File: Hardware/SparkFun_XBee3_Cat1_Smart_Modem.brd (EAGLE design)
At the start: 45.7 x 63.5 mm, 138 parts, among them J1 USB Female Type C Connector, J3 USB Female Type C Connector, J4 QWIIC_RIGHT_ANGLE, Q2 3.1A/30V/105mΩ, U1 FSUSB30MUX_MSOP10, U2 AP63203, U3 ESD Diode, U5 ESD Diode, U7 FT231XS

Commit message: Adds a few more vias
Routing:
- net GND: vias 80 -> 82
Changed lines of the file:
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@@
 <via x="17.1196" y="15.0368" extent="1-16" drill="0.3048"/>
 <via x="27.9146" y="15.0622" extent="1-16" drill="0.3048"/>
+<via x="27.6606" y="13.6906" extent="1-16" drill="0.3048"/>
+<via x="30.0482" y="12.6492" extent="1-16" drill="0.3048"/>
 </signal>
 <signal name="3.3V">
@@
 <wire x1="27.94" y1="33.401" x2="28.0924" y2="33.401" width="0.762" layer="16"/>
 <wire x1="28.0924" y1="33.401" x2="28.8544" y2="32.639" width="0.762" layer="16"/>
-<wire x1="30.099" y1="26.543" x2="29.7948" y2="29.21" width="0" layer="19" extent="1-1"/>
-<wire x1="33.108" y1="21.971" x2="33.147" y2="23.114" width="0" layer="19" extent="1-1"/>
-<wire x1="13.12" y1="19.304" x2="13.081" y2="20.447" width="0" layer="19" extent="1-1"/>
-<wire x1="28.917" y1="25.781" x2="30.099" y2="25.654" width="0" layer="19" extent="1-1"/>
-<wire x1="31.662" y1="13.589" x2="30.48" y2="13.589" width="0" layer="19" extent="1-1"/>
-<wire x1="28.917" y1="24.2824" x2="30.099" y2="24.638" width="0" layer="19" extent="1-1"/>
-<wire x1="33.3375" y1="20.4597" x2="33.108" y2="21.971" width="0" layer="19" extent="1-1"/>
-<wire x1="31.4325" y1="15.1003" x2="31.662" y2="13.589" width="0" layer="19" extent="1-1"/>
-<wire x1="30.7975" y1="15.1003" x2="31.4325" y2="15.1003" width="0" layer="19" extent="1-1"/>
-<wire x1="30.1625" y1="15.1003" x2="30.7975" y2="15.1003" width="0" layer="19" extent="1-1"/>
-<wire x1="13.12" y1="17.78" x2="13.12" y2="19.304" width="0" layer="19" extent="1-1"/>
 </signal>
 <signal name="V_USB">
@@
 <vertex x="23.622" y="29.591"/>
 </polygon>
-<wire x1="26.6448" y1="29.21" x2="26.25" y2="32.512" width="0" layer="19" extent="1-1"/>
-<wire x1="24.2351" y1="29.21" x2="26.6448" y2="29.21" width="0" layer="19" extent="1-1"/>
 </signal>
 <signal name="EN">

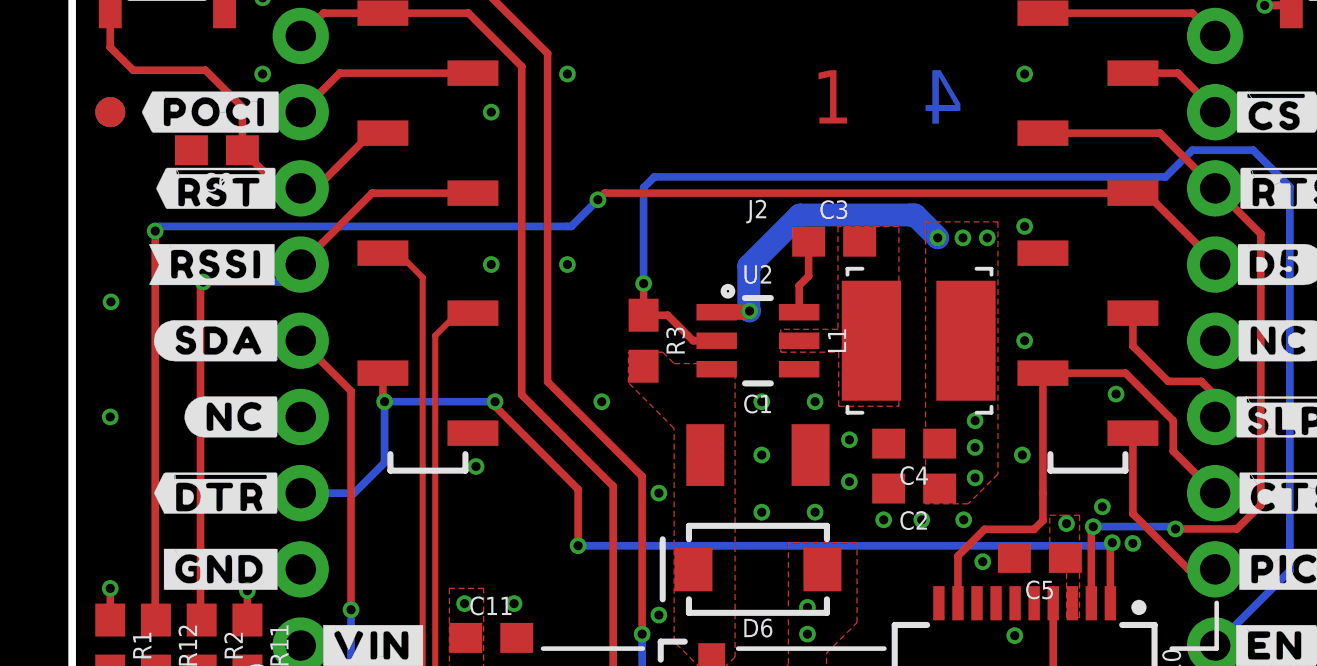
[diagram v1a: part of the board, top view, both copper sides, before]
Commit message: Updates inductor to one with a higher saturation rating
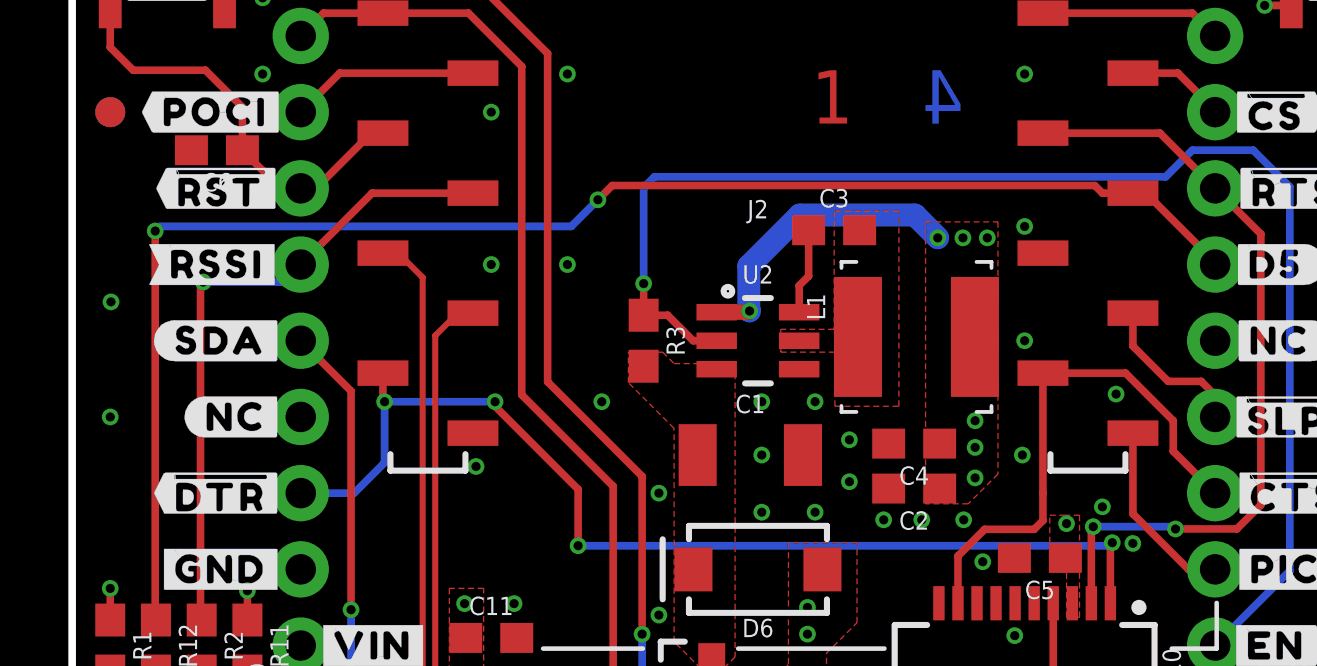
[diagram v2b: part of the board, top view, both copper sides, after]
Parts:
- L1: value 3.9uH -> 3.9UH
- moved C3 0.38 mm to (25.4, 32.9)
- moved C1 0.25 mm to (22.6, 25.4)
- moved L1 0.14 mm to (28.2, 29.3), turned to 270 degrees
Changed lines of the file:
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@@
 <setting verticaltext="up"/>
 </settings>
-<grid distance="0.05" unitdist="inch" unit="inch" style="dots" multiple="1" display="yes" altdistance="0.001" altunitdist="inch" altunit="inch"/>
+<grid distance="0.05" unitdist="inch" unit="inch" style="dots" multiple="1" display="yes" altdistance="0.005" altunitdist="inch" altunit="inch"/>
 <layers>
 <layer number="1" name="Top" color="4" fill="1" visible="yes" active="yes"/>
@@
 <layer number="39" name="tKeepout" color="4" fill="11" visible="yes" active="yes"/>
 <layer number="40" name="bKeepout" color="1" fill="11" visible="no" active="yes"/>
-<layer number="41" name="tRestrict" color="4" fill="10" visible="no" active="yes"/>
+<layer number="41" name="tRestrict" color="4" fill="10" visible="yes" active="yes"/>
 <layer number="42" name="bRestrict" color="1" fill="10" visible="no" active="yes"/>
 <layer number="43" name="vRestrict" color="2" fill="10" visible="no" active="yes"/>
@@
 <wire x1="25.146" y1="1.524" x2="26.67" y2="0" width="0.2032" layer="20" curve="-90"/>
 <text x="24.257" y="1.905" size="1.27" layer="16" font="vector" ratio="15" rot="MR0">v10</text>
-<rectangle x1="27.8384" y1="32.8422" x2="28.0924" y2="33.0962" layer="41"/>
+<rectangle x1="27.8384" y1="33.0962" x2="28.0924" y2="33.3502" layer="41"/>
 <text x="20.447" y="0.381" size="0.762" layer="46" font="vector" ratio="15">Route Out</text>
 <dimension x1="38.1" y1="44.45" x2="0" y2="44.45" x3="19.05" y3="74.93" textsize="1.778" textratio="15" layer="47" unit="inch"/>
@@
 <attribute name="VALUE" x="22.86" y="26.67" size="0.6096" layer="27" font="vector" ratio="20" align="bottom-center"/>
 </element>
-<element name="L1" library="SparkFun-Coils" package="INDUCTOR_3.9UH" value="3.9uH" x="28.2448" y="29.21" smashed="yes" rot="R90">
-<attribute name="NAME" x="25.8028" y="29.21" size="0.6096" layer="25" font="vector" ratio="20" rot="R90" align="bottom-center"/>
-<attribute name="PROD_ID" value="NDUC-18014" x="25.7048" y="22.86" size="1.778" layer="27" rot="R90" display="off"/>
-<attribute name="VALUE" value="3.9uH" x="30.6578" y="29.21" size="0.6096" layer="27" font="vector" ratio="20" rot="R90" align="top-center"/>
-</element>
-<element name="C3" library="SparkFun-Capacitors" package="0603" value="0.1uF" x="25.4" y="32.512" smashed="yes">
-<attribute name="NAME" x="25.4" y="33.274" size="0.6096" layer="25" font="vector" ratio="20" align="bottom-center"/>
-<attribute name="PROD_ID" value="CAP-08604" x="13.97" y="35.052" size="1.778" layer="27" display="off"/>
-<attribute name="VALUE" x="25.4" y="31.75" size="0.6096" layer="27" font="vector" ratio="20" align="top-center"/>
+<element name="C3" library="SparkFun-Capacitors" package="0603" value="0.1uF" x="25.4" y="32.893" smashed="yes">
+<attribute name="NAME" x="25.4" y="33.655" size="0.6096" layer="25" font="vector" ratio="20" align="bottom-center"/>
+<attribute name="PROD_ID" value="CAP-08604" x="13.97" y="35.433" size="1.778" layer="27" display="off"/>
+<attribute name="VALUE" x="25.4" y="32.131" size="0.6096" layer="27" font="vector" ratio="20" align="top-center"/>
 </element>
 <element name="C2" library="SparkFun-Capacitors" package="0603" value="22uF" x="28.067" y="24.2824" smashed="yes" rot="R180">
@@
 <attribute name="VALUE" x="28.067" y="26.543" size="0.6096" layer="27" font="vector" ratio="20" rot="R180" align="top-center"/>
 </element>
-<element name="C1" library="SparkFun-Capacitors" package="1210" value="10uF" x="22.86" y="25.4" smashed="yes">
-<attribute name="NAME" x="22.86" y="26.797" size="0.6096" layer="25" font="vector" ratio="20" align="bottom-center"/>
-<attribute name="PROD_ID" value="CAP-09824" x="12.7" y="8.89" size="1.778" layer="27" display="off"/>
-<attribute name="VALUE" x="22.86" y="24.003" size="0.6096" layer="27" font="vector" ratio="20" align="top-center"/>
+<element name="C1" library="SparkFun-Capacitors" package="1210" value="10uF" x="22.606" y="25.4" smashed="yes">
+<attribute name="NAME" x="22.606" y="26.797" size="0.6096" layer="25" font="vector" ratio="20" align="bottom-center"/>
+<attribute name="PROD_ID" value="CAP-09824" x="12.446" y="8.89" size="1.778" layer="27" display="off"/>
+<attribute name="VALUE" x="22.606" y="24.003" size="0.6096" layer="27" font="vector" ratio="20" align="top-center"/>
 </element>
 <element name="R3" library="SparkFun-Resistors" package="0603" value="10k" x="19.05" y="29.21" smashed="yes" rot="R270">
@@
 <attribute name="PROD_ID" value="CAP-00810" x="32.258" y="21.971" size="1.778" layer="27" font="vector" ratio="15" rot="R180" display="off"/>
 <attribute name="VALUE" x="32.258" y="22.733" size="0.6096" layer="27" font="vector" ratio="20" rot="R180" align="top-center"/>
+</element>
+<element name="L1" library="SparkFun-Coils" package="INDUCTOR_3.9UH" value="3.9UH" x="28.194" y="29.337" smashed="yes" rot="R270">
+<attribute name="NAME" x="24.494" y="30.787" size="0.6096" layer="25" font="vector" ratio="20" rot="R270"/>
+<attribute name="VALUE" x="31.194" y="31.037" size="0.6096" layer="27" font="vector" ratio="20" rot="R270"/>
 </element>
 </elements>
@@
 <contactref element="J4" pad="2"/>
 <contactref element="R11" pad="1"/>
-<contactref element="L1" pad="P$2"/>
 <contactref element="C4" pad="1"/>
 <contactref element="C2" pad="1"/>
@@
 <wire x1="22.5806" y1="30.2006" x2="22.5552" y2="30.226" width="0.762" layer="16"/>
 <wire x1="22.5552" y1="31.6992" x2="22.5552" y2="30.226" width="0.762" layer="16"/>
-<wire x1="24.257" y1="33.401" x2="27.94" y2="33.401" width="0.762" layer="16"/>
+<wire x1="24.257" y1="33.401" x2="28.0924" y2="33.401" width="0.762" layer="16"/>
 <contactref element="J6" pad="1"/>
 <wire x1="22.5552" y1="31.6992" x2="24.257" y2="33.401" width="0.762" layer="16"/>
@@
 <contactref element="U7" pad="14"/>
 <contactref element="U7" pad="13"/>
-<wire x1="27.94" y1="33.401" x2="28.0924" y2="33.401" width="0.762" layer="16"/>
 <wire x1="28.0924" y1="33.401" x2="28.8544" y2="32.639" width="0.762" layer="16"/>
+<contactref element="L1" pad="P$2"/>
 </signal>
 <signal name="V_USB">
@@
 <contactref element="J2" pad="15"/>
 <via x="17.526" y="33.909" extent="1-16" drill="0.3048"/>
-<wire x1="35.36" y1="34.13" x2="17.747" y2="34.13" width="0.254" layer="1"/>
-<wire x1="17.526" y1="33.909" x2="17.747" y2="34.13" width="0.254" layer="1"/>
+<wire x1="35.36" y1="34.13" x2="34.344" y2="34.13" width="0.254" layer="1"/>
+<wire x1="34.344" y1="34.13" x2="34.09" y2="34.384" width="0.254" layer="1"/>
+<wire x1="34.09" y1="34.384" x2="18.001" y2="34.384" width="0.254" layer="1"/>
+<wire x1="17.526" y1="33.909" x2="18.001" y2="34.384" width="0.254" layer="1"/>
 <contactref element="J5" pad="6"/>
 <wire x1="38.1" y1="31.8218" x2="35.7918" y2="34.13" width="0.254" layer="1"/>
@@
 <wire x1="2.794" y1="19.9" x2="2.7686" y2="19.9254" width="0.254" layer="1"/>
 <via x="2.7686" y="32.8676" extent="1-16" drill="0.3048"/>
-<wire x1="16.51" y1="33.02" x2="2.921" y2="33.02" width="0.254" layer="16"/>
+<wire x1="16.637" y1="33.02" x2="2.921" y2="33.02" width="0.254" layer="16"/>
 <wire x1="2.7686" y1="32.8676" x2="2.921" y2="33.02" width="0.254" layer="16"/>
 <wire x1="35.36" y1="34.13" x2="35.7918" y2="34.13" width="0.254" layer="1"/>
 <wire x1="17.526" y1="33.909" x2="16.637" y2="33.02" width="0.254" layer="16"/>
-<wire x1="16.637" y1="33.02" x2="16.51" y2="33.02" width="0.254" layer="16"/>
 </signal>
 <signal name="D6/!RTS!">
@@
 <contactref element="U2" pad="6"/>
 <contactref element="C3" pad="1"/>
-<wire x1="24.55" y1="32.512" x2="24.55" y2="31.3639" width="0.254" layer="1"/>
+<wire x1="24.55" y1="32.893" x2="24.55" y2="31.3639" width="0.254" layer="1"/>
 <wire x1="24.55" y1="31.3639" x2="24.2351" y2="31.049" width="0.254" layer="1"/>
 <wire x1="24.2351" y1="30.16" x2="24.2351" y2="31.049" width="0.254" layer="1"/>
@@
 <signal name="N$8">
 <contactref element="U2" pad="5"/>
-<contactref element="L1" pad="P$1"/>
 <contactref element="C3" pad="2"/>
 <polygon width="0.127" layer="1" thermals="no">
 <vertex x="23.622" y="28.829"/>
-<vertex x="25.5524" y="28.829"/>
-<vertex x="25.5524" y="27.0256"/>
+<vertex x="25.4254" y="28.829"/>
+<vertex x="25.4254" y="27.0256"/>
 <vertex x="27.559" y="27.0256"/>
-<vertex x="27.559" y="33.02"/>
-<vertex x="25.527" y="33.02"/>
-<vertex x="25.527" y="29.591"/>
+<vertex x="27.559" y="33.528"/>
+<vertex x="25.4" y="33.528"/>
+<vertex x="25.4" y="29.591"/>
 <vertex x="23.622" y="29.591"/>
 </polygon>
+<contactref element="L1" pad="P$1"/>
 </signal>
 <signal name="EN">
